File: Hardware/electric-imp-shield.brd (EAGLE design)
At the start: 59.7 x 53.3 mm, 39 parts, among them Q2 BSS138, Q3 BSS138, U1 ELECTRIC_IMP, U2 ARDUINO_SHIELD, U3 MIC5219-3.3, U4 ATSHA204-TSU

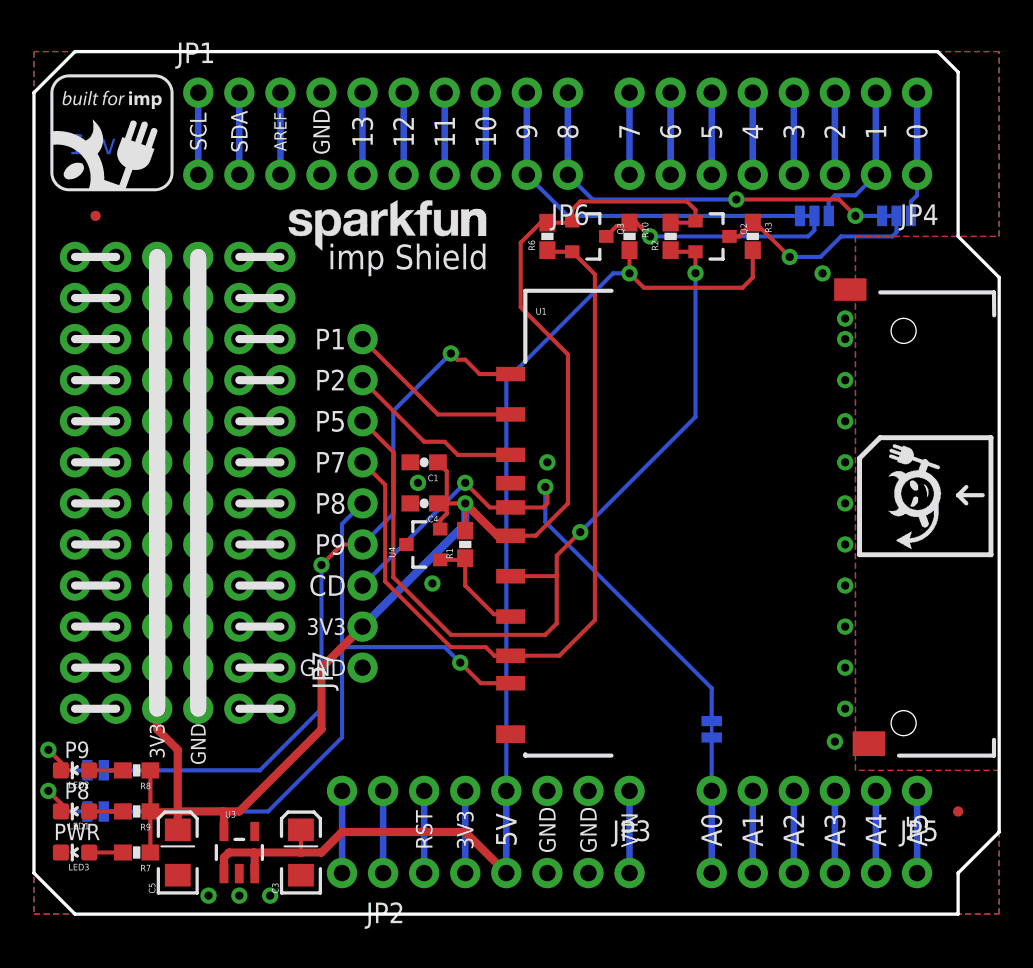
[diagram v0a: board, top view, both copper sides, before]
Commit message: removed micro fids, added regulars
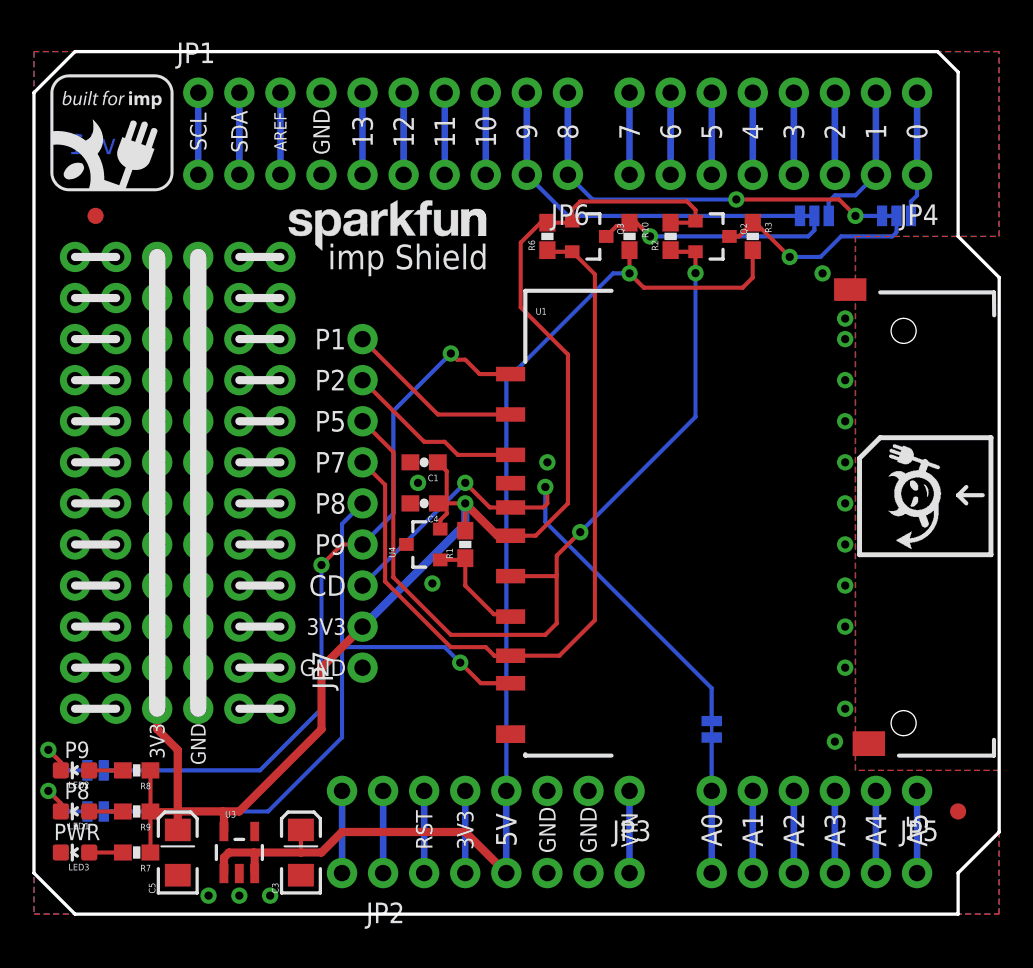
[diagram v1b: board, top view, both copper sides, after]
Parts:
- removed JP8, JP9: FIDUCIALUFIDUCIAL, SparkFun:MICRO-FIDUCIAL
- added FID1, FID2: FIDUCIAL1X2, SparkFun-Aesthetics:FIDUCIAL-1X2
